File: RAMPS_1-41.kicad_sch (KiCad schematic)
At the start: 85 parts, among them J1 282837-6, J2 Conn_01x02, J3 Conn_01x03, J4 Conn_01x06, J5 Conn_01x04, Q1 STP55NF06L, Q2 STP55NF06L, Q3 STP55NF06L, U1 ARDUINO_MEGA_SHIELD, U2 A4988BREAKOUT, U3 A4988BREAKOUT, U4 A4988BREAKOUT, U5 A4988BREAKOUT, U6 A4988BREAKOUT, X4 MSTBA4

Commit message: Update symbols
Updated all the rescue symbols and deleted the cache files
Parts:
- C1, C10, C3, C4, C5, C6, C7, C8, C9: symbol RAMPS_1-41-rescue:CP1-Device -> Device:C_Polarized_US

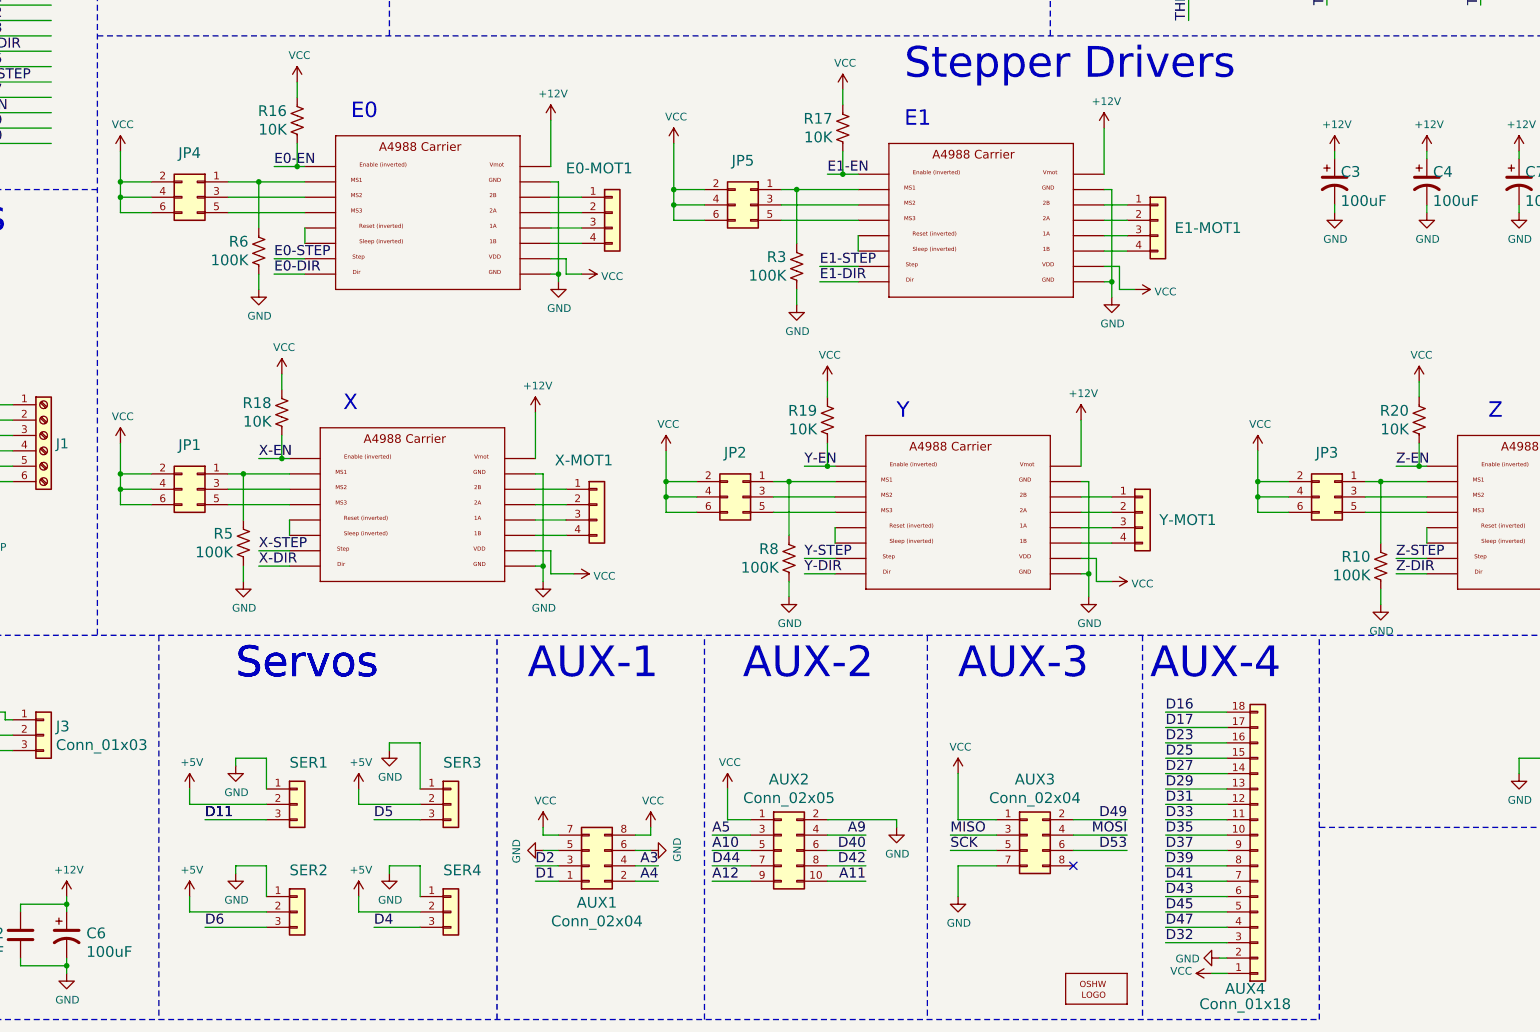
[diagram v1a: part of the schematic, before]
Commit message: TMC updates
Added closed solder jumpers to ~Reset and ~Sleep to make it easier to use Trinamic SPI drivers.
Updated A4988 symbol to Trinamic SPI pin names in parathesis.
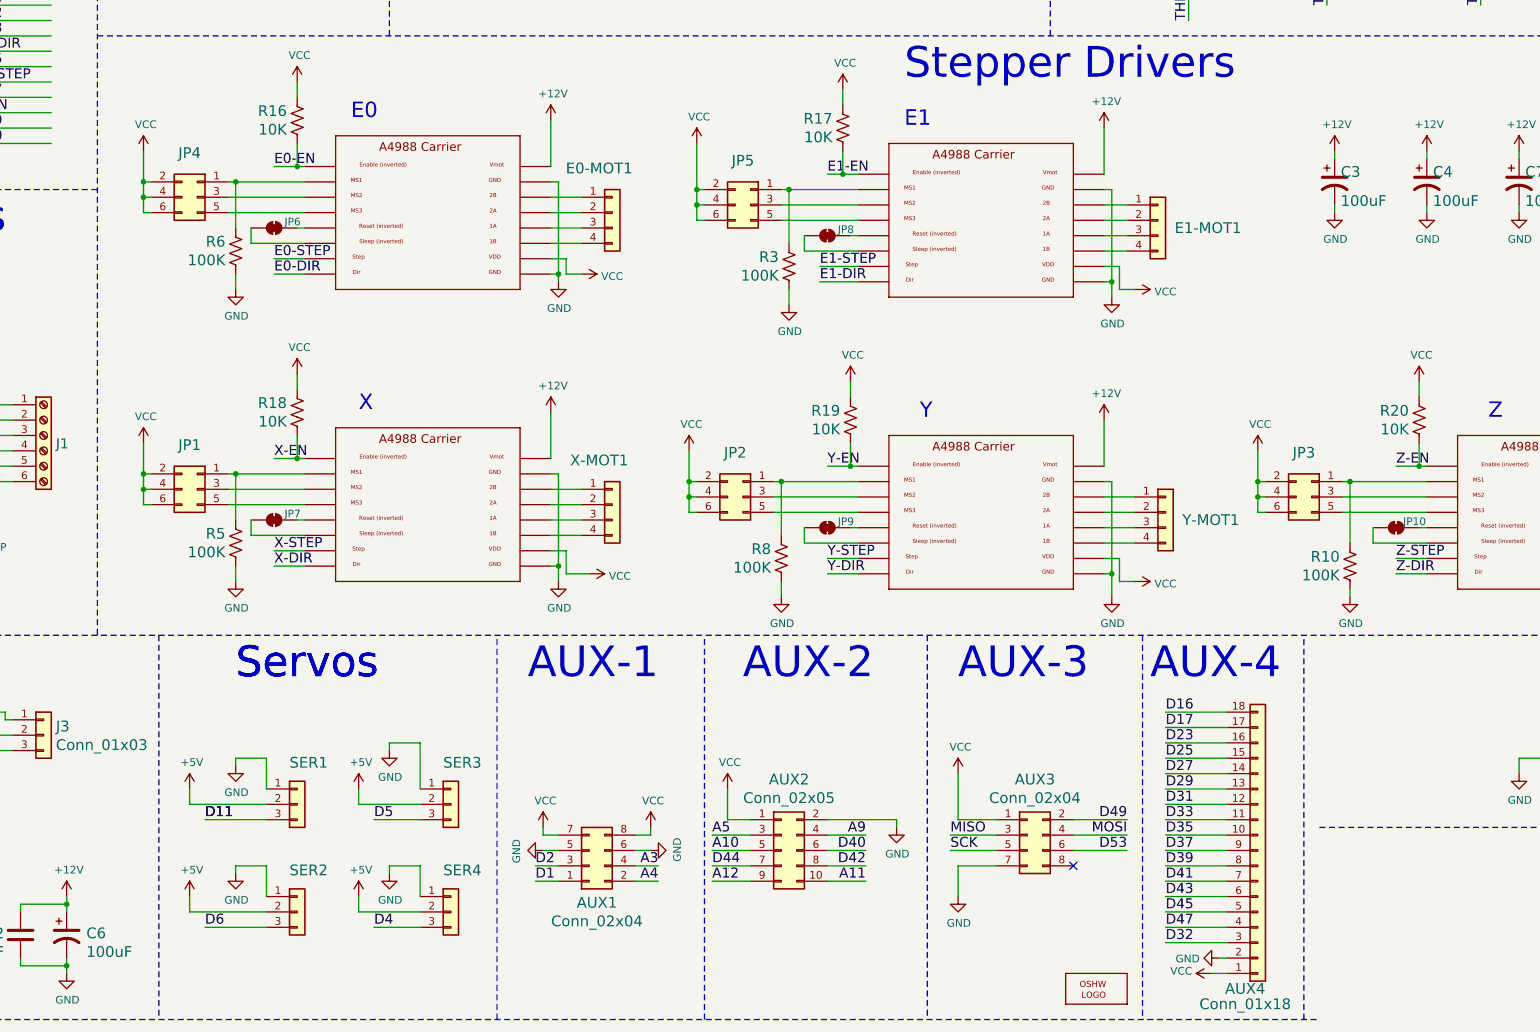
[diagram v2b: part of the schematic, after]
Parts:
- added JP10, JP6, JP7, JP8, JP9: ~, symbol Jumper:SolderJumper_2_Bridged
- U2, U3, U4, U5, U6: footprint RAMPS_1-41:A4988_BREAKOUT -> REPRAPJR_A4988BREAKOUT
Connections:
- net at U5.RST: now also JP6.2 (B); no longer U5.SLP (SLEEP)
- net at U6.RST: now also JP8.2 (B); no longer U6.SLP (SLEEP)
- net at U2.RST: now also JP7.2 (B); no longer U2.SLP (SLEEP)
- net at U3.RST: now also JP9.2 (B); no longer U3.SLP (SLEEP)
- net at U4.RST: now also JP10.2 (B); no longer U4.SLP (SLEEP)
- new net: JP6.1 (A), U5.SLP (SLEEP)
- new net: JP8.1 (A), U6.SLP (SLEEP)
- new net: JP7.1 (A), U2.SLP (SLEEP)
- new net: JP9.1 (A), U3.SLP (SLEEP)
- new net: JP10.1 (A), U4.SLP (SLEEP)
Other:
- moved on the sheet: JP3, R10, R18, R19, R3, R5, R6, R8, X-MOT1, Y-MOT1
